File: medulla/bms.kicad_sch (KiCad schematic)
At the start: 35 parts, among them Q1 CSD18534Q5A, Q2 CSD18534Q5A, U1 BQ7791504PW

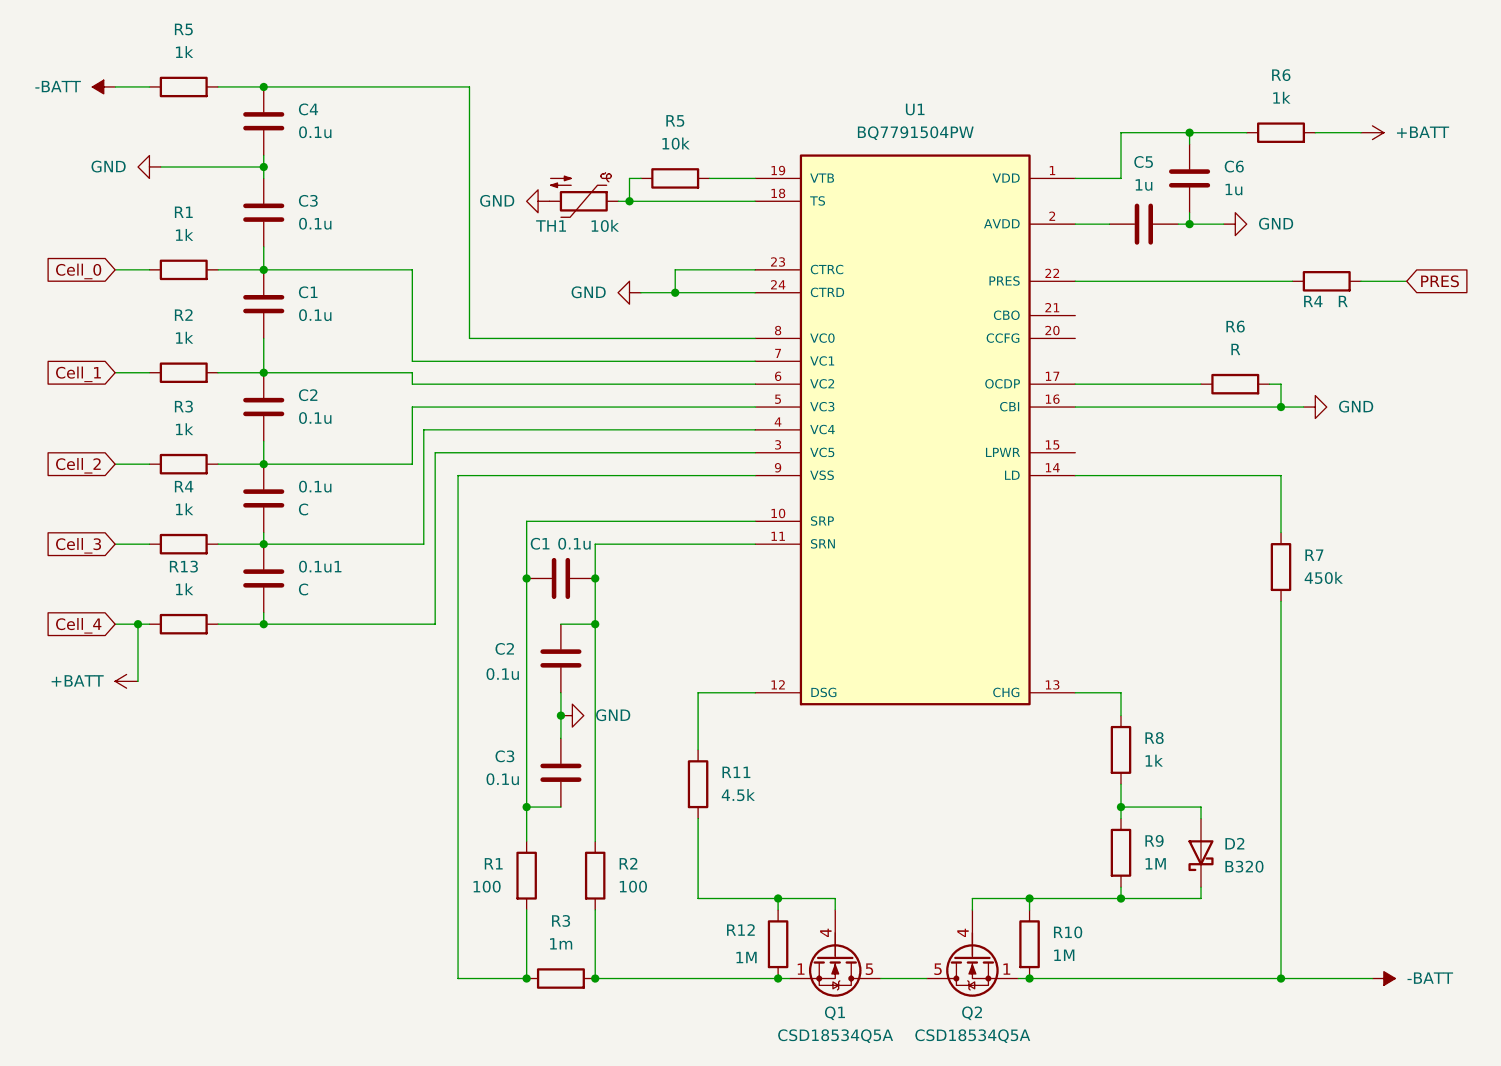
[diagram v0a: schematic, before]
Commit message: alpha 0.2.0: Added RP2040, LM2936-3.3V Regulator, removed ADS1115, PCA9685
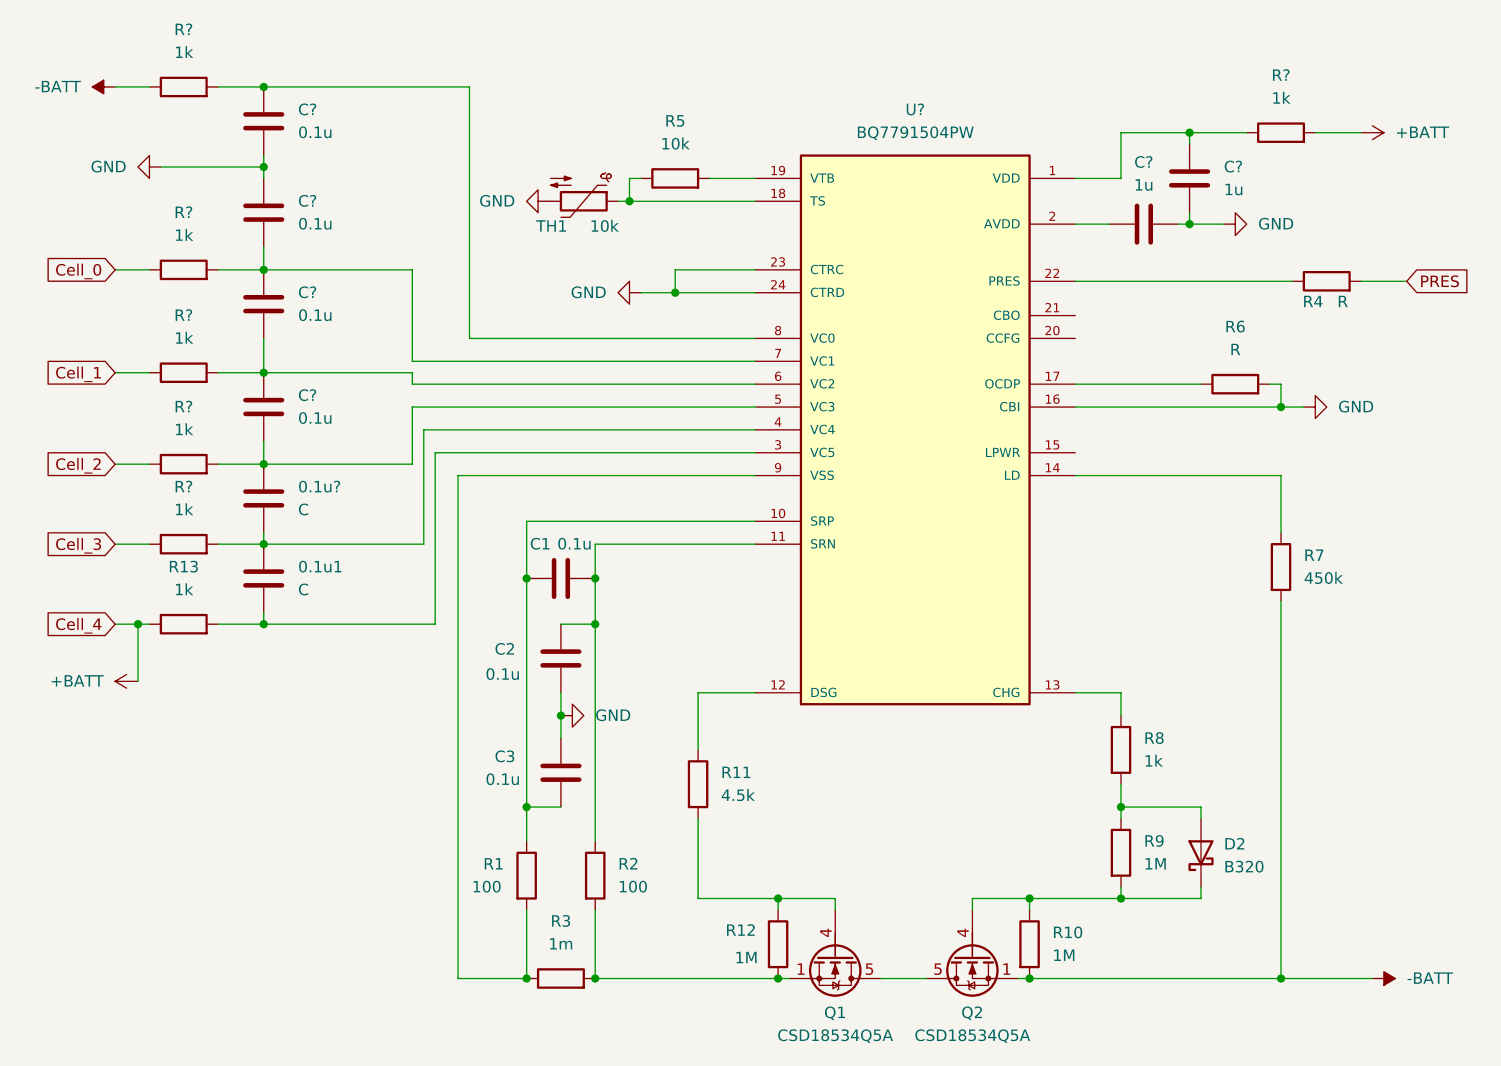
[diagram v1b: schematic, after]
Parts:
- renumbered 0.1u to 0.1u?, C4 to C?, C2 to C?, C3 to C?, C6 to C?, C1 to C?, C5 to C?, R2 to R?, R5 to R?, R4 to R?, R3 to R?, R1 to R?, R6 to R?, U1 to U?
